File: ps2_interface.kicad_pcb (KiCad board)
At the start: 4 copper layers, 83.3 x 34.3 mm, 28 parts, among them J1 Mini-DIN-6, J2 Conn_01x13, J3 KBD, U1 74HC595, U2 74HC595, U3 74HC180, U4 74HC08, U5 74HC14

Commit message: Update
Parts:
- removed TP1: REG_CLK, TestPoint:TestPoint_Loop_D2.60mm_Drill1.6mm_Beaded
- removed TP2: LATCH_CLK, TestPoint:TestPoint_Loop_D2.60mm_Drill1.6mm_Beaded
- removed U3: 74HC180, Package_DIP:DIP-14_W7.62mm
- added U6: 74HC280, Package_DIP:DIP-14_W7.62mm, F.Cu at (115.1, 72.9)
- J1: footprint AK's_Footprints:PS2_mini_din_6 -> AK's Footprints:PS2_mini_din_6
- J2: footprint Connector_PinSocket_2.54mm:PinSocket_1x13_P2.54mm_Vertical -> Connector_PinHeader_2.54mm:PinHeader_1x13_P2.54mm_Vertical; moved to B.Cu
- moved TP3 11.0 mm to (148.3, 67.6)
- moved C1 8.97 mm to (150.2, 81.8)
- moved D1 8.64 mm to (156.7, 72.6)
- moved J1 6.49 mm to (75.8, 77.0), turned to 90 degrees
- moved J3 2.64 mm to (86.3, 64.0), turned to 0 degrees
- moved C6 2.54 mm to (133.6, 69.8), turned to 180 degrees
- moved C4 2.54 mm to (111.8, 69.8), turned to 180 degrees
- moved C3 2.54 mm to (100.8, 69.8), turned to 180 degrees
- moved C7 2.50 mm to (144.5, 69.8), turned to 180 degrees
- moved C2 2.32 mm to (90.4, 75.7), turned to -90 degrees
- moved C5 2.29 mm to (122.7, 69.8), turned to 180 degrees
- moved R1 0.57 mm to (149.1, 77.2)
- turned J2 to -90 degrees
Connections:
- D1 pad 2: Net-(D1-Pad2) -> Net-(D1-A)
- R1 pad 1: Net-(D1-Pad2) -> Net-(D1-A)
- U4 pad 1: /DE -> Net-(U4-Pad1)
- U4 pad 10: Net-(U4-Pad10) -> Net-(U6-Odd)
- U4 pad 11: Net-(U4-Pad10) -> Net-(U4-Pad11)
- U4 pad 12: VCC -> /DE
- U4 pad 13: /~{REG_CLK} -> Net-(U4-Pad13)
- U4 pad 2: Net-(U4-Pad2) -> Net-(U4-Pad1)
- U4 pad 3: Net-(U4-Pad3) -> /~{LATCH_CLK}
- U4 pad 4: Net-(U4-Pad3) -> /~{REG_CLK}
- U4 pad 5: Net-(U3-Pad5) -> /~{REG_CLK}
- U4 pad 6: /VALID_PACKET -> Net-(U4-Pad1)
- U4 pad 8: /~{LATCH_CLK} -> /VALID_PACKET
- U4 pad 9: VCC -> Net-(U4-Pad11)
- U5 pad 10: /~{REG_OE} -> Net-(D1-A)
- U5 pad 11: /BUS_ENABLE -> /KBD_CLK
- U5 pad 2: Net-(U4-Pad2) -> Net-(U4-Pad13)
- U5 pad 3: /KBD_CLK -> /BUS_ENABLE
- U5 pad 4: Net-(D1-Pad2) -> /~{REG_OE}
- U5 pad 8: Net-(U3-Pad4) -> unconnected-(U5-Pad8)
- U5 pad 9: /DP -> VCC
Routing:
- net GND: track 0.00 -> 275.5 mm, vias 38 -> 0
- net /DP: track 69.3 -> 22.9 mm, vias 1 -> 0
- net Net-(U3-Pad4): track 34.5 -> 0.00 mm
- net /~{LATCH_CLK}: track 54.9 -> 28.8 mm, vias 1 -> 0
- net Net-(D1-Pad2): track 22.6 -> 0.00 mm
- net /~{REG_CLK}: track 70.6 -> 49.2 mm, vias 1 -> 0
- net Net-(U6-Odd): track 0.00 -> 19.6 mm
- net VCC: track 144.7 -> 127.0 mm
- net /D0: track 56.7 -> 39.9 mm, vias 0 -> 1
- net /D7: track 35.6 -> 49.5 mm, vias 0 -> 1
- net Net-(U4-Pad1): track 0.00 -> 13.6 mm
- net Net-(D1-A): track 0.00 -> 12.3 mm
- net Net-(U4-Pad2): track 11.9 -> 0.00 mm
- net Net-(U3-Pad5): track 11.9 -> 0.00 mm
- net /D1: track 43.4 -> 31.8 mm, vias 0 -> 1
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- removed copper zone on B.Cu, net GND
- removed copper zone on F.Cu, net GND
- removed copper zone on In1.Cu, net GND
- removed copper zone on In2.Cu, net GND
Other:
- copper layers 4 -> 2
- board text added: "74HC280"
- board text added: "PS/2 interface v1.2 Adrien Kohlbecker 2023-06-21"
- board text removed: "74HC180"
- board text removed: "PS/2 interface v1.1 Adrien Kohlbecker 2021-05-18"

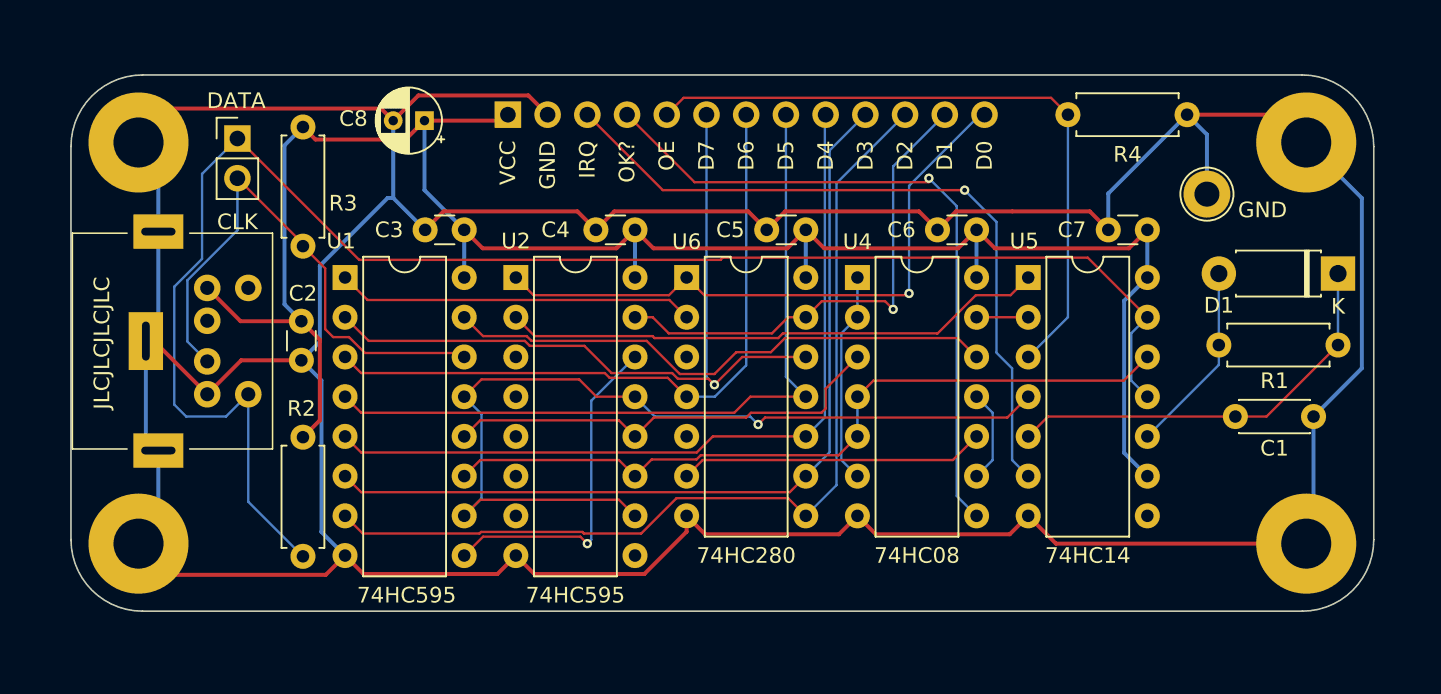
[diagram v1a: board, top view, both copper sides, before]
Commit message: Add auto reset
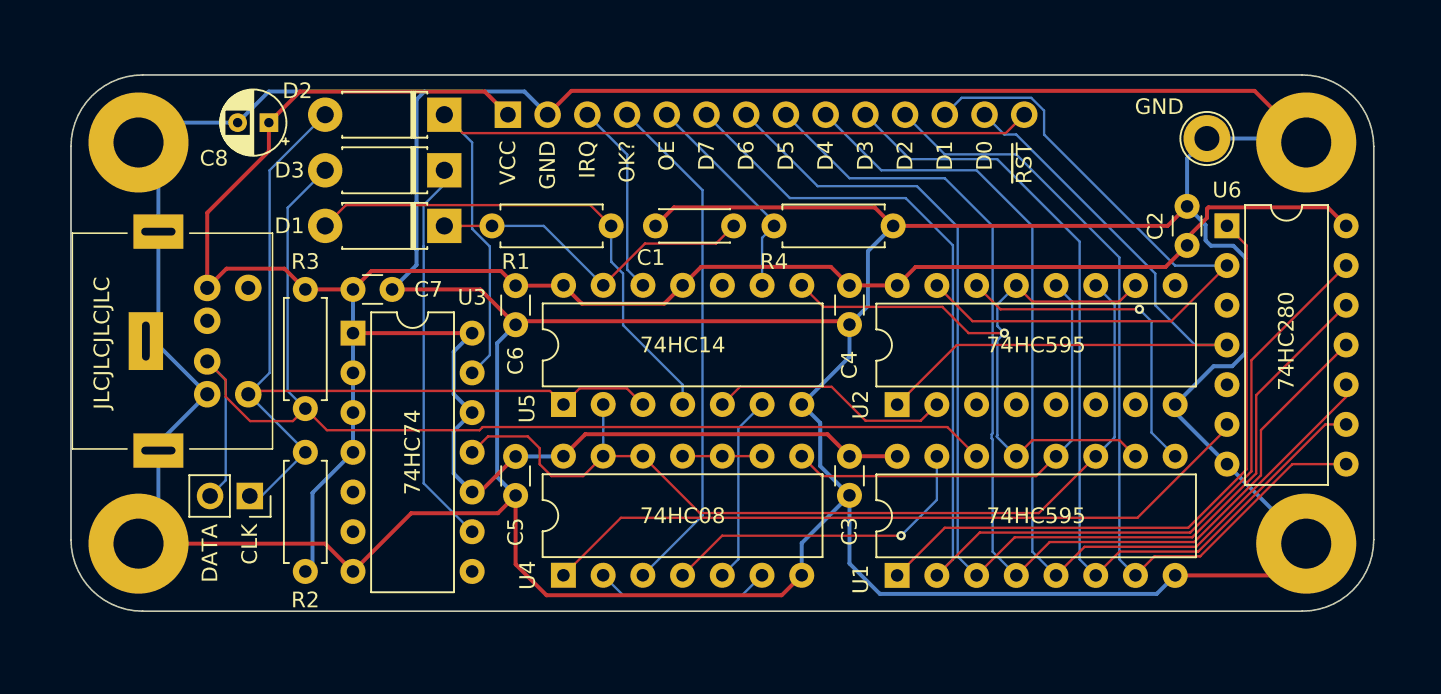
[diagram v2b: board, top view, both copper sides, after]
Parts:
- added D2: 1N5817, Diode_THT:D_DO-41_SOD81_P7.62mm_Horizontal, F.Cu at (99.6, 62.5)
- added D3: 1N5817, Diode_THT:D_DO-41_SOD81_P7.62mm_Horizontal, F.Cu at (99.6, 66.0)
- added U3: 74HC74, Package_DIP:DIP-14_W7.62mm, F.Cu at (93.7, 76.5)
- J2: value Conn_01x13 -> Conn_01x14; footprint Connector_PinHeader_2.54mm:PinHeader_1x13_P2.54mm_Vertical -> Connector_PinHeader_2.54mm:PinHeader_1x14_P2.54mm_Vertical
- J3: footprint Connector_PinHeader_2.54mm:PinHeader_1x02_P2.54mm_Vertical -> Connector_PinSocket_2.54mm:PinSocket_1x02_P2.54mm_Vertical
- moved D1 57.2 mm to (99.6, 69.6)
- moved C2 56.8 mm to (147.1, 70.8), turned to 90 degrees
- moved C7 50.9 mm to (93.7, 73.7), turned to 0 degrees
- moved U1 40.1 mm to (128.5, 91.9), turned to 90 degrees
- moved R1 39.6 mm to (110.2, 69.6), turned to 180 degrees
- moved U6 34.7 mm to (149.6, 69.6)
- moved C1 34.3 mm to (118.1, 69.6), turned to 180 degrees
- moved U5 30.8 mm to (107.2, 81.0), turned to 90 degrees
- moved C6 29.7 mm to (104.1, 73.4), turned to -90 degrees
- moved C3 28.6 mm to (125.5, 84.3), turned to -90 degrees
- moved U4 26.8 mm to (107.2, 91.9), turned to 90 degrees
- moved U2 25.7 mm to (128.5, 81.0), turned to 90 degrees
- moved C5 23.5 mm to (104.1, 84.3), turned to -90 degrees
- moved J3 22.9 mm to (87.1, 86.9), turned to -90 degrees
- moved R4 20.1 mm to (120.7, 69.6)
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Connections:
- U4 pad 1: Net-(U4-Pad1) -> Net-(U6-Odd)
- U4 pad 10: Net-(U6-Odd) -> Net-(U4-Pad10)
- U4 pad 11: Net-(U4-Pad11) -> Net-(U4-Pad10)
- U4 pad 12: /DE -> /~{REG_CLK}
- U4 pad 13: Net-(U4-Pad13) -> /~{REG_CLK}
- U4 pad 2: Net-(U4-Pad1) -> Net-(U4-Pad2)
- U4 pad 3: /~{LATCH_CLK} -> /VALID_PACKET
- U4 pad 4: /~{REG_CLK} -> /DE
- U4 pad 5: /~{REG_CLK} -> Net-(U4-Pad5)
- U4 pad 6: Net-(U4-Pad1) -> Net-(U4-Pad2)
- U4 pad 8: /VALID_PACKET -> /~{LATCH_CLK}
- U4 pad 9: Net-(U4-Pad11) -> Net-(U4-Pad10)
- U5 pad 1: /DS -> /KBD_CLK
- U5 pad 10: Net-(D1-A) -> unconnected-(U5-Pad10)
- U5 pad 11: /KBD_CLK -> VCC
- U5 pad 12: /~{REG_CLK} -> /IRQ
- U5 pad 13: /KBD_CLK -> Net-(D1-K)
- U5 pad 2: Net-(U4-Pad13) -> /~{REG_CLK}
- U5 pad 3: /BUS_ENABLE -> /KBD_CLK
- U5 pad 4: /~{REG_OE} -> Net-(D1-A)
- U5 pad 5: Net-(D1-K) -> /DS
- U5 pad 6: /IRQ -> Net-(U4-Pad5)
- U5 pad 8: unconnected-(U5-Pad8) -> /~{REG_OE}
- U5 pad 9: VCC -> /BUS_ENABLE
- U6 pad 1: /D0 -> /DP
- U6 pad 12: /D7 -> /D6
- U6 pad 13: /D1 -> /D7
- U6 pad 2: /DP -> /D1
- U6 pad 4: /D6 -> /D0
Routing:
- net GND: track 275.5 -> 343.5 mm
- net /~{RST}: track 0.00 -> 56.2 mm
- net /KBD_CLK: track 105.1 -> 55.3 mm
- net VCC: track 127.0 -> 175.4 mm
- net /KBD_DATA: track 34.7 -> 79.4 mm
- net /IRQ: track 46.1 -> 12.4 mm, vias 1 -> 0
- net /D7: track 49.5 -> 79.3 mm, vias 1 -> 0
- net /D6: track 43.6 -> 73.0 mm
- net /BUS_ENABLE: track 43.1 -> 13.8 mm
- net Net-(U6-Odd): track 19.6 -> 46.3 mm
- net Net-(D3-K): track 0.00 -> 24.1 mm
- net Net-(D1-A): track 12.3 -> 32.7 mm
- net /DS: track 34.9 -> 15.5 mm
- net /D5: track 48.9 -> 68.1 mm
- net /DP: track 22.9 -> 41.3 mm
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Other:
- board text added: "74HC74"
- board text added: "~{RST}"
